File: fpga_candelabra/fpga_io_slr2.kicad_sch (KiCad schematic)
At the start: 1 part, among them U1 XCVU13P-B2104

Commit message: fpga_candelabra: sch & layout v0.5, pass basic ERC & DRC
Signed-off-by: Yichuan Gao <gaoyichuan000@gmail.com>
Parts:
- added C343: 47uF 6.3V, Capacitor_SMD:C_0603_1608Metric, symbol Device:C_Small
- added C344: 10uF 6.3V, Capacitor_SMD:C_0402_1005Metric, symbol Device:C_Small
- added R193: 240R 1%, Resistor_SMD:R_0402_1005Metric, symbol Device:R_Small
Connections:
- net FMC.LA01_CC+ is gone; now on net FMC.LA04+: U1.BE8 (IO_L2P_T0L_N2_68)
- net FMC.LA01_CC- is gone; now on net FMC.LA04-: U1.BF8 (IO_L2N_T0L_N3_68)
- net FMC.LA05+ is gone; now on net FMC.LA07+: U1.BD9 (IO_L6P_T0U_N10_AD6P_68)
- net FMC.LA05- is gone; now on net FMC.LA07-: U1.BD8 (IO_L6N_T0U_N11_AD6N_68)
- net FMC.LA09+ is gone; now on net FMC.LA00_CC+: U1.BA7 (IO_L10P_T1U_N6_QBC_AD4P_68)
- net FMC.LA09- is gone; now on net FMC.LA00_CC-: U1.BB7 (IO_L10N_T1U_N7_QBC_AD4N_68)
- net FMC.LA00_CC+: no longer U1.BE7 (IO_L1P_T0L_N0_DBC_68)
- net FMC.LA00_CC-: no longer U1.BF7 (IO_L1N_T0L_N1_DBC_68)
- net FMC.LA02+: now also U1.BE7 (IO_L1P_T0L_N0_DBC_68); no longer U1.BF10 (IO_L3P_T0L_N4_AD15P_68)
- net FMC.LA02-: now also U1.BF7 (IO_L1N_T0L_N1_DBC_68); no longer U1.BF9 (IO_L3N_T0L_N5_AD15N_68)
- net FMC.LA03+: now also U1.BC8 (IO_L9P_T1L_N4_AD12P_68); no longer U1.BE11 (IO_L4P_T0U_N6_DBC_AD7P_68)
- net FMC.LA03-: now also U1.BC7 (IO_L9N_T1L_N5_AD12N_68); no longer U1.BE10 (IO_L4N_T0U_N7_DBC_AD7N_68)
- net FMC.LA04+: no longer U1.BE12 (IO_L5P_T0U_N8_AD14P_68)
- net FMC.LA04-: no longer U1.BF12 (IO_L5N_T0U_N9_AD14N_68)
- net FMC.LA07+: no longer U1.BB11 (IO_L8P_T1L_N2_AD5P_68)
- net FMC.LA07-: no longer U1.BB10 (IO_L8N_T1L_N3_AD5N_68)
- net FMC.LA08+: now also U1.BA9 (IO_L12P_T1U_N10_GC_68); no longer U1.BC8 (IO_L9P_T1L_N4_AD12P_68)
- net FMC.LA08-: now also U1.BA8 (IO_L12N_T1U_N11_GC_68); no longer U1.BC7 (IO_L9N_T1L_N5_AD12N_68)
- net FMC.LA11+: now also U1.BF10 (IO_L3P_T0L_N4_AD15P_68); no longer U1.BA9 (IO_L12P_T1U_N10_GC_68)
- net FMC.LA11-: now also U1.BF9 (IO_L3N_T0L_N5_AD15N_68); no longer U1.BA8 (IO_L12N_T1U_N11_GC_68)
- net FMC0_VADJ: now also C343.1, C344.1
- net QSFP0.~{MODPRS}: now also U1.H27 (IO_L11P_T1U_N8_GC_71)
- net QSFP0.~{RXLOS}: now also U1.F28 (IO_L16P_T2U_N6_QBC_AD3P_71)
- net QSFP1.~{MODPRS}: now also U1.K28 (IO_L8N_T1L_N3_AD5N_71)
- net QSFP1.~{RXLOS}: now also U1.L29 (IO_L7N_T1L_N1_QBC_AD13N_71)
- net ~{SYS_RST}: now reaches U1.A30 (IO_L24N_T3U_N11_71)
- net MBUS.AN: now reaches U1.C28 (IO_T3U_N12_71)
- net MBUS.SCK: now reaches U1.C29 (IO_L20N_T3L_N3_AD1N_71)
- net MBUS.RST: now reaches U1.D28 (IO_L18N_T2U_N11_AD2N_71)
- net MBUS.MISO: now reaches U1.D29 (IO_L20P_T3L_N2_AD1P_71)
- net MCU_U0TXD: now reaches U1.D30 (IO_L21N_T3L_N5_AD8N_71)
- net MBUS.RX: now reaches U1.E26 (IO_T2U_N12_71)
- net MBUS.PWM: now reaches U1.E27 (IO_L17N_T2U_N9_AD10N_71)
- net MBUS.CS: now reaches U1.E28 (IO_L18P_T2U_N10_AD2P_71)
- net MCU_U0RXD: now reaches U1.E30 (IO_L21P_T3L_N4_AD8P_71)
- net MBUS.INT: now reaches U1.F27 (IO_L17P_T2U_N8_AD10P_71)
- net MBUS.MOSI: now reaches U1.F29 (IO_L16N_T2U_N7_QBC_AD3N_71)
- net QSFP0.SCL: now reaches U1.G27 (IO_L14N_T2L_N3_GC_71)
- net MBUS.SCL: now reaches U1.G29 (IO_L15N_T2L_N5_AD11N_71)
- net MBUS.SDA: now reaches U1.H28 (IO_L11N_T1U_N9_GC_71)
- net MBUS.TX: now reaches U1.H29 (IO_L15P_T2L_N4_AD11P_71)
- net SYS_CLK+: now reaches U1.J28 (IO_L12P_T1U_N10_GC_71)
- net SYS_CLK-: now reaches U1.J29 (IO_L12N_T1U_N11_GC_71)
- net QSFP0.SDA: now reaches U1.K27 (IO_L10N_T1U_N7_QBC_AD4N_71)
- net QSFP1.SDA: now reaches U1.L27 (IO_L9N_T1L_N5_AD12N_71)
- net QSFP1.SCL: now reaches U1.L28 (IO_L8P_T1L_N2_AD5P_71)
- net VRP_68: now reaches U1.BD10 (IO_T0U_N12_VRP_68)
- net VRP_68: now also R193.2
- net FMC.LA06+ renamed FMC.LA20+
- net FMC.LA06- renamed FMC.LA20-
- net FMC.LA10+ renamed FMC.LA12+
- net FMC.LA10- renamed FMC.LA12-
- new net Earth: C343.2, C344.2, R193.1
- new net FMC.LA15+: U1.BE11 (IO_L4P_T0U_N6_DBC_AD7P_68)
- new net FMC.LA15-: U1.BE10 (IO_L4N_T0U_N7_DBC_AD7N_68)
- new net FMC.LA16+: U1.BB11 (IO_L8P_T1L_N2_AD5P_68)
- new net FMC.LA16-: U1.BB10 (IO_L8N_T1L_N3_AD5N_68)
- new net FMC.LA19+: U1.BE12 (IO_L5P_T0U_N8_AD14P_68)
- new net FMC.LA19-: U1.BF12 (IO_L5N_T0U_N9_AD14N_68)
- no-connect marks 2 -> 135

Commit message: fpga_candelabra: more bugfixes & improvements for rev 0.2.0
- Add Digilent JTAG-SMT2-NC onboard
- Add fan controller & 4pin fan header
- Use 9pin header for USB2.0
- Misc fixes for structure

Signed-off-by: Yichuan Gao <gaoyichuan000@gmail.com>
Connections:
- net SMT3_UART.CTS: now reaches U1.M27 (IO_L9P_T1L_N4_AD12P_71)
- net SMT3_UART.RTS: now reaches U1.M29 (IO_L7P_T1L_N0_QBC_AD13P_71)
- net SMT3_UART.TXD: now reaches U1.N28 (IO_L5N_T0U_N9_AD14N_71)
- net SMT3_UART.RXD: now reaches U1.N29 (IO_L4N_T0U_N7_DBC_AD7N_71)
- no-connect marks 135 -> 131

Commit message: fpga_candelabra: add author & rev to schematics
Signed-off-by: Yichuan Gao <gaoyichuan000@gmail.com>
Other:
- company: (none) -> CHIPS Alliance
- title: (none) -> FPGA SLR2 IO
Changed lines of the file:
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@@
 	(generator_version "8.0")
 	(paper "A4")
+	(title_block
+		(title "FPGA SLR2 IO")
+		(date "2025-02-05")
+		(rev "0.2.0")
+		(company "CHIPS Alliance")
+		(comment 1 "Yichuan Gao")
+		(comment 2 "Yichuan Gao")
+	)
 	(junction
 		(at 45.72 129.54)

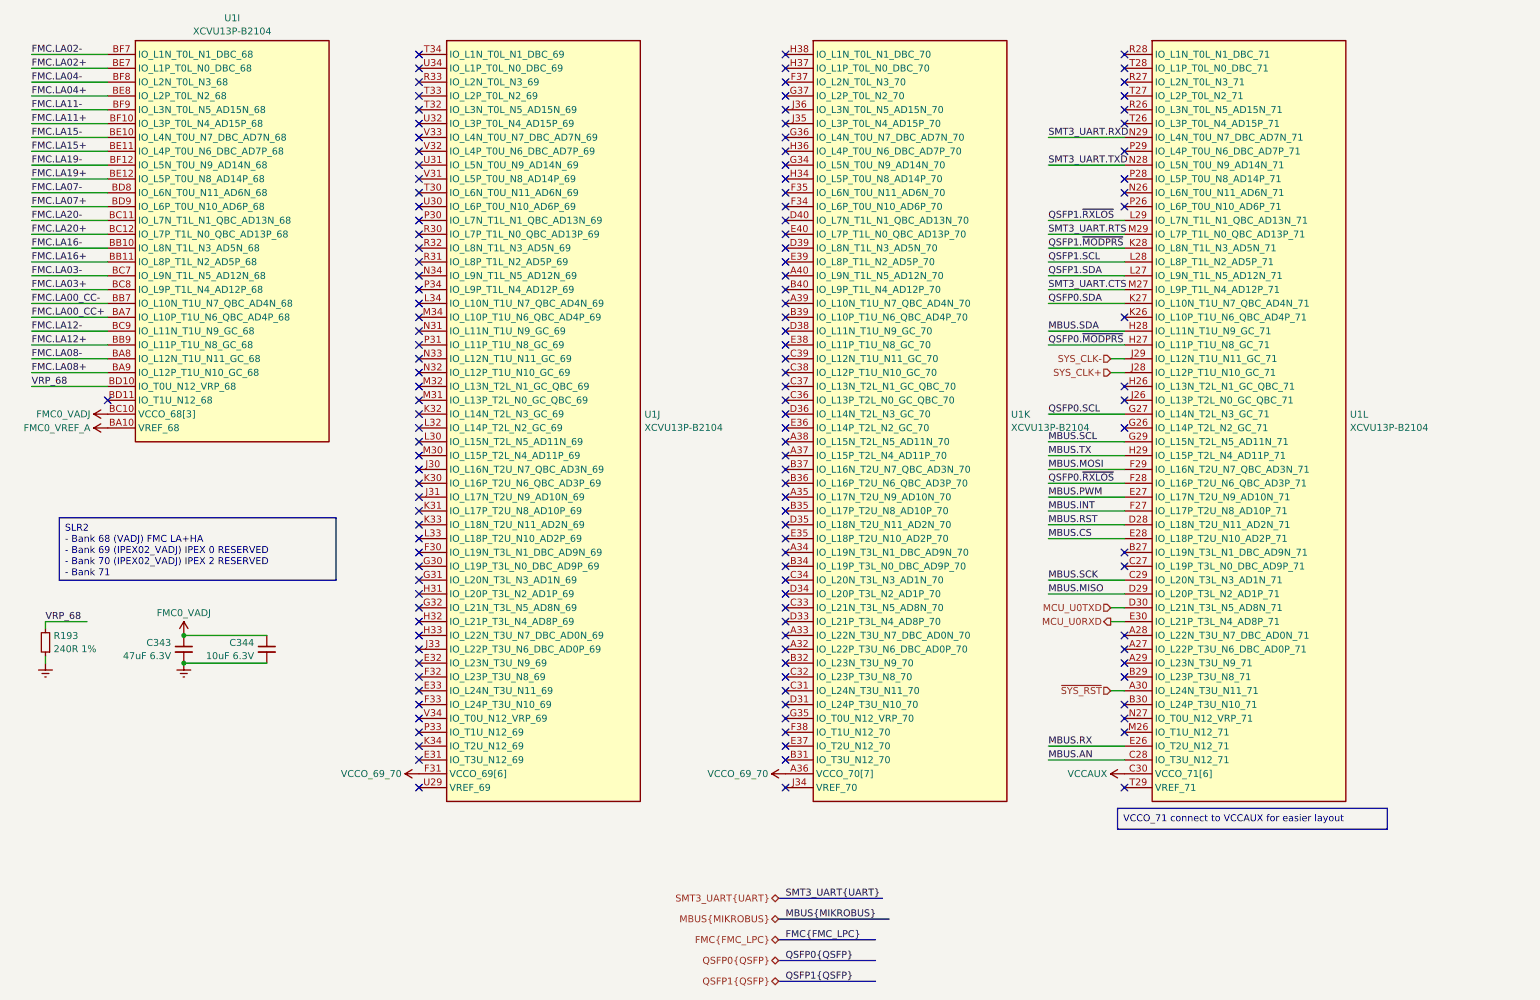
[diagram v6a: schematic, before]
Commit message: fpga_candelabra: update to kicad 9.0
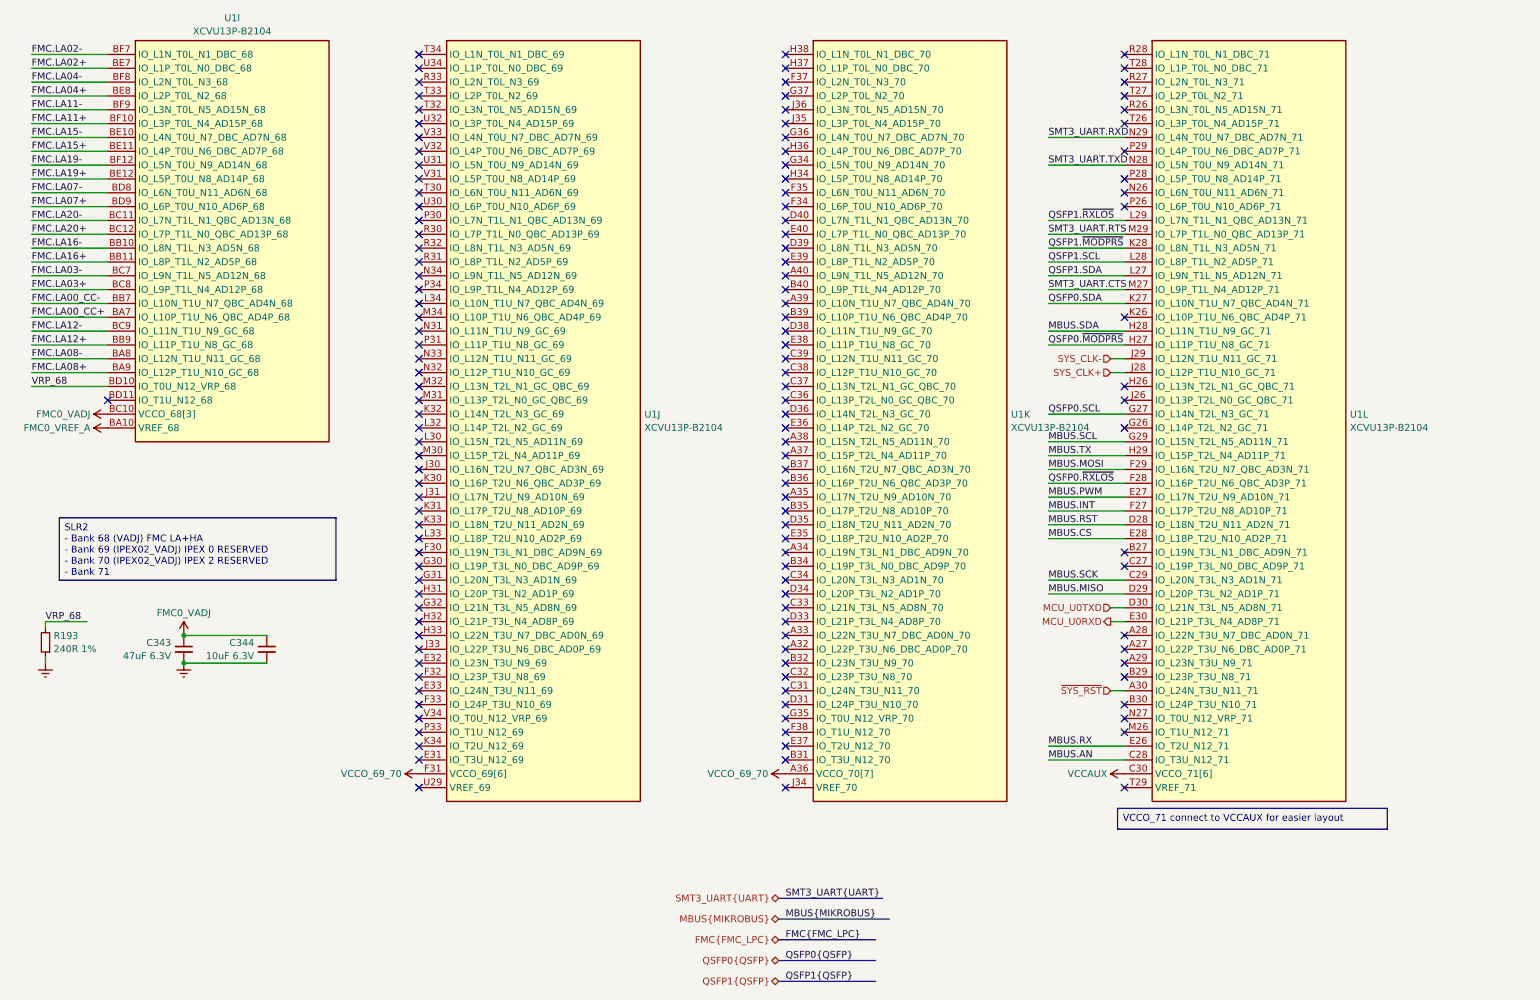
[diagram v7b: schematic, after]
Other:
- company: CHIPS Alliance -> Sipeed
